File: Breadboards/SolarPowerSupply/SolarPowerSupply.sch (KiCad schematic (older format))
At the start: 47 parts

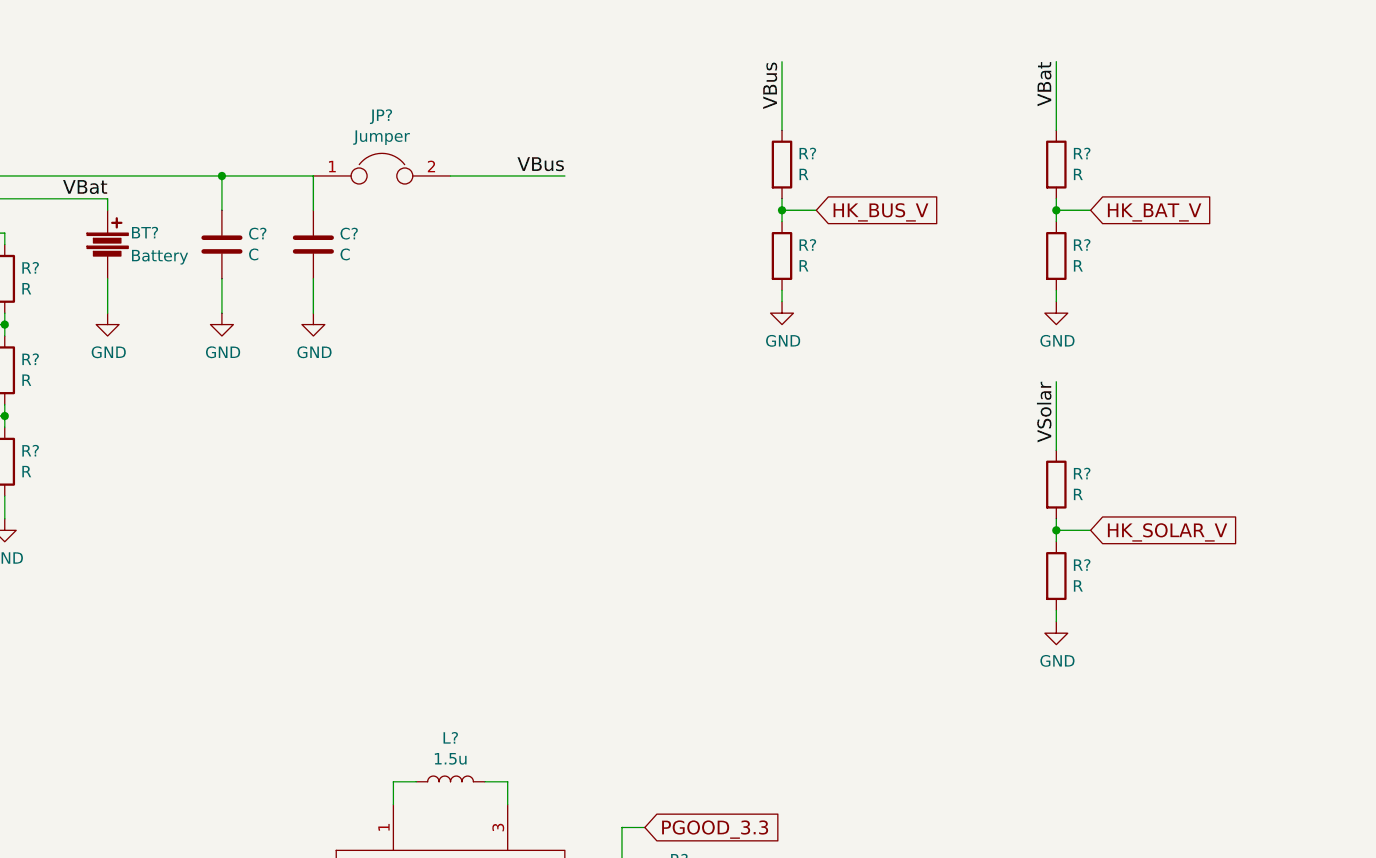
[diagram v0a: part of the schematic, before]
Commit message: Adds Connectors for Power and HK
- One Connector added with 5V, 3.3V and GND
- One Connector added with all HK lines
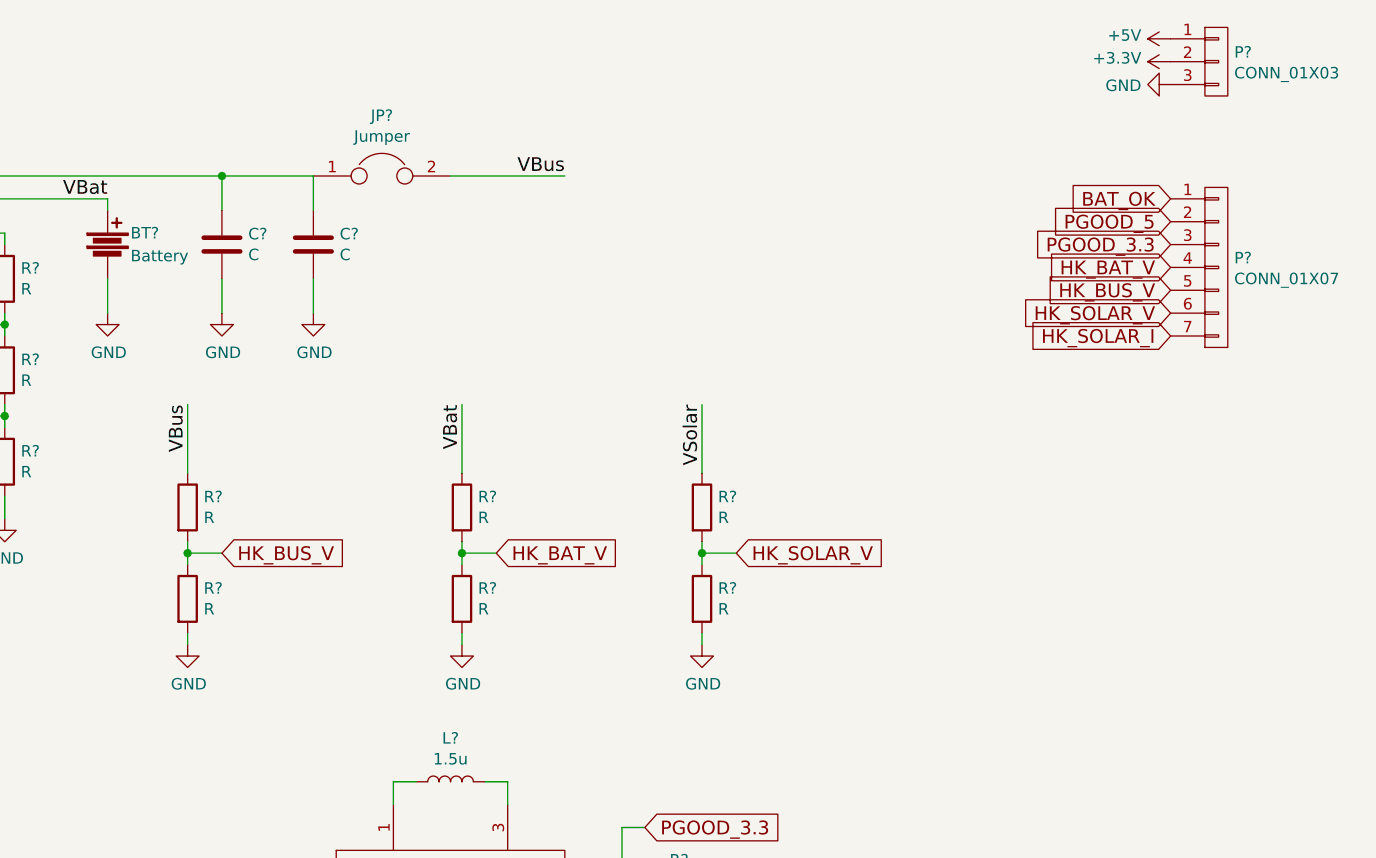
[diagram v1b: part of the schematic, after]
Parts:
- added P?: CONN_01X03, symbol CONN_01X03
- added P?: CONN_01X07, symbol CONN_01X07
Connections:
- net +3V3: now also P?.2 (P2)
- net +5V: now also P?.1 (P1)
- net BAT_OK: now also P?.1 (P1)
- net GND: now also P?.3 (P3)
- net HK_BAT_V: now also P?.4 (P4)
- net HK_BUS_V: now also P?.5 (P5)
- net HK_SOLAR_I: now also P?.7 (P7)
- net HK_SOLAR_V: now also P?.6 (P6)
- net PGOOD_3.3: now also P?.3 (P3)
- net PGOOD_5: now also P?.2 (P2)
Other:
- moved on the sheet: R?
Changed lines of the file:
@@
 L R R?
 U 1 1 5A132406
-P 8650 1600
-F 0 "R?" H 8720 1646 50  0000 L CNN
-F 1 "R" H 8720 1555 50  0000 L CNN
-F 2 "" V 8580 1600 50  0001 C CNN
-F 3 "" H 8650 1600 50  0001 C CNN
-	1    8650 1600
+P 6050 3100
+F 0 "R?" H 6120 3146 50  0000 L CNN
+F 1 "R" H 6120 3055 50  0000 L CNN
+F 2 "" V 5980 3100 50  0001 C CNN
+F 3 "" H 6050 3100 50  0001 C CNN
+	1    6050 3100
 	1    0    0    -1
 $EndComp
@@
 L R R?
 U 1 1 5A132407
-P 8650 2000
-F 0 "R?" H 8720 2046 50  0000 L CNN
-F 1 "R" H 8720 1955 50  0000 L CNN
-F 2 "" V 8580 2000 50  0001 C CNN
-F 3 "" H 8650 2000 50  0001 C CNN
-	1    8650 2000
-	1    0    0    -1
-$EndComp
-Wire Wire Line
-	8650 1150 8650 1450
-Wire Wire Line
-	8650 1750 8650 1850
-Wire Wire Line
-	8650 2150 8650 2200
+P 6050 3500
+F 0 "R?" H 6120 3546 50  0000 L CNN
+F 1 "R" H 6120 3455 50  0000 L CNN
+F 2 "" V 5980 3500 50  0001 C CNN
+F 3 "" H 6050 3500 50  0001 C CNN
+	1    6050 3500
+	1    0    0    -1
+$EndComp
+Wire Wire Line
+	6050 2650 6050 2950
+Wire Wire Line
+	6050 3250 6050 3350
+Wire Wire Line
+	6050 3650 6050 3700
 $Comp
 L GND #PWR?
 U 1 1 5A132408
-P 8650 2200
-F 0 "#PWR?" H 8650 1950 50  0001 C CNN
-F 1 "GND" H 8655 2027 50  0000 C CNN
-F 2 "" H 8650 2200 50  0001 C CNN
-F 3 "" H 8650 2200 50  0001 C CNN
-	1    8650 2200
-	1    0    0    -1
-$EndComp
-Text GLabel 8800 1800 2    60   Input ~ 0
+P 6050 3700
+F 0 "#PWR?" H 6050 3450 50  0001 C CNN
+F 1 "GND" H 6055 3527 50  0000 C CNN
+F 2 "" H 6050 3700 50  0001 C CNN
+F 3 "" H 6050 3700 50  0001 C CNN
+	1    6050 3700
+	1    0    0    -1
+$EndComp
+Text GLabel 6200 3300 2    60   Input ~ 0
 HK_BUS_V
 Wire Wire Line
-	8650 1800 8800 1800
-Connection ~ 8650 1800
-Text Label 8650 1150 3    60   ~ 0
+	6050 3300 6200 3300
+Connection ~ 6050 3300
+Text Label 6050 2650 3    60   ~ 0
 VBus
 $Comp
 L R R?
 U 1 1 5A132409
-P 9850 1600
-F 0 "R?" H 9920 1646 50  0000 L CNN
-F 1 "R" H 9920 1555 50  0000 L CNN
-F 2 "" V 9780 1600 50  0001 C CNN
-F 3 "" H 9850 1600 50  0001 C CNN
-	1    9850 1600
+P 7250 3100
+F 0 "R?" H 7320 3146 50  0000 L CNN
+F 1 "R" H 7320 3055 50  0000 L CNN
+F 2 "" V 7180 3100 50  0001 C CNN
+F 3 "" H 7250 3100 50  0001 C CNN
+	1    7250 3100
 	1    0    0    -1
 $EndComp
@@
 L R R?
 U 1 1 5A13240A
-P 9850 2000
-F 0 "R?" H 9920 2046 50  0000 L CNN
-F 1 "R" H 9920 1955 50  0000 L CNN
-F 2 "" V 9780 2000 50  0001 C CNN
-F 3 "" H 9850 2000 50  0001 C CNN
-	1    9850 2000
-	1    0    0    -1
-$EndComp
-Wire Wire Line
-	9850 1150 9850 1450
-Wire Wire Line
-	9850 1750 9850 1850
-Wire Wire Line
-	9850 2150 9850 2200
+P 7250 3500
+F 0 "R?" H 7320 3546 50  0000 L CNN
+F 1 "R" H 7320 3455 50  0000 L CNN
+F 2 "" V 7180 3500 50  0001 C CNN
+F 3 "" H 7250 3500 50  0001 C CNN
+	1    7250 3500
+	1    0    0    -1
+$EndComp
+Wire Wire Line
+	7250 2650 7250 2950
+Wire Wire Line
+	7250 3250 7250 3350
+Wire Wire Line
+	7250 3650 7250 3700
 $Comp
 L GND #PWR?
 U 1 1 5A13240B
-P 9850 2200
-F 0 "#PWR?" H 9850 1950 50  0001 C CNN
-F 1 "GND" H 9855 2027 50  0000 C CNN
-F 2 "" H 9850 2200 50  0001 C CNN
-F 3 "" H 9850 2200 50  0001 C CNN
-	1    9850 2200
-	1    0    0    -1
-$EndComp
-Text GLabel 10000 1800 2    60   Input ~ 0
+P 7250 3700
+F 0 "#PWR?" H 7250 3450 50  0001 C CNN
+F 1 "GND" H 7255 3527 50  0000 C CNN
+F 2 "" H 7250 3700 50  0001 C CNN
+F 3 "" H 7250 3700 50  0001 C CNN
+	1    7250 3700
+	1    0    0    -1
+$EndComp
+Text GLabel 7400 3300 2    60   Input ~ 0
 HK_BAT_V
 Wire Wire Line
-	9850 1800 10000 1800
-Connection ~ 9850 1800
-Text Label 9850 1150 3    60   ~ 0
+	7250 3300 7400 3300
+Connection ~ 7250 3300
+Text Label 7250 2650 3    60   ~ 0
 VBat
 $Comp
 L R R?
 U 1 1 5A13240C
-P 9850 3000
-F 0 "R?" H 9920 3046 50  0000 L CNN
-F 1 "R" H 9920 2955 50  0000 L CNN
-F 2 "" V 9780 3000 50  0001 C CNN
-F 3 "" H 9850 3000 50  0001 C CNN
-	1    9850 3000
+P 8300 3100
+F 0 "R?" H 8370 3146 50  0000 L CNN
+F 1 "R" H 8370 3055 50  0000 L CNN
+F 2 "" V 8230 3100 50  0001 C CNN
+F 3 "" H 8300 3100 50  0001 C CNN
+	1    8300 3100
 	1    0    0    -1
 $EndComp
@@
 L R R?
 U 1 1 5A13240D
-P 9850 3400
-F 0 "R?" H 9920 3446 50  0000 L CNN
-F 1 "R" H 9920 3355 50  0000 L CNN
-F 2 "" V 9780 3400 50  0001 C CNN
-F 3 "" H 9850 3400 50  0001 C CNN
-	1    9850 3400
-	1    0    0    -1
-$EndComp
-Wire Wire Line
-	9850 2550 9850 2850
-Wire Wire Line
-	9850 3150 9850 3250
-Wire Wire Line
-	9850 3550 9850 3600
+P 8300 3500
+F 0 "R?" H 8370 3546 50  0000 L CNN
+F 1 "R" H 8370 3455 50  0000 L CNN
+F 2 "" V 8230 3500 50  0001 C CNN
+F 3 "" H 8300 3500 50  0001 C CNN
+	1    8300 3500
+	1    0    0    -1
+$EndComp
+Wire Wire Line
+	8300 2650 8300 2950
+Wire Wire Line
+	8300 3250 8300 3350
+Wire Wire Line
+	8300 3650 8300 3700
 $Comp
 L GND #PWR?
 U 1 1 5A13240E
-P 9850 3600
-F 0 "#PWR?" H 9850 3350 50  0001 C CNN
-F 1 "GND" H 9855 3427 50  0000 C CNN
-F 2 "" H 9850 3600 50  0001 C CNN
-F 3 "" H 9850 3600 50  0001 C CNN
-	1    9850 3600
-	1    0    0    -1
-$EndComp
-Text GLabel 10000 3200 2    60   Input ~ 0
+P 8300 3700
+F 0 "#PWR?" H 8300 3450 50  0001 C CNN
+F 1 "GND" H 8305 3527 50  0000 C CNN
+F 2 "" H 8300 3700 50  0001 C CNN
+F 3 "" H 8300 3700 50  0001 C CNN
+	1    8300 3700
+	1    0    0    -1
+$EndComp
+Text GLabel 8450 3300 2    60   Input ~ 0
 HK_SOLAR_V
 Wire Wire Line
-	9850 3200 10000 3200
-Connection ~ 9850 3200
-Text Label 9850 2550 3    60   ~ 0
+	8300 3300 8450 3300
+Connection ~ 8300 3300
+Text Label 8300 2650 3    60   ~ 0
 VSolar
 Text Notes -1050 2700 0    60   Italic 0
@@
 Wire Wire Line
 	1650 3950 1650 4050
+$Comp
+L CONN_01X03 P?
+U 1 1 5A1337CA
+P 10550 1150
+F 0 "P?" H 10628 1191 50  0000 L CNN
+F 1 "CONN_01X03" H 10628 1100 50  0000 L CNN
+F 2 "" H 10550 1150 50  0000 C CNN
+F 3 "" H 10550 1150 50  0000 C CNN
+	1    10550 1150
+	1    0    0    -1
+$EndComp
+$Comp
+L +3.3V #PWR?
+U 1 1 5A1339BF
+P 10350 1150
+F 0 "#PWR?" H 10350 1000 50  0001 C CNN
+F 1 "+3.3V" V 10365 1278 50  0000 L CNN
+F 2 "" H 10350 1150 50  0000 C CNN
+F 3 "" H 10350 1150 50  0000 C CNN
+	1    10350 1150
+	0    -1   -1   0
+$EndComp
+$Comp
+L +5V #PWR?
+U 1 1 5A133B1D
+P 10350 1050
+F 0 "#PWR?" H 10350 900 50  0001 C CNN
+F 1 "+5V" V 10365 1178 50  0000 L CNN
+F 2 "" H 10350 1050 50  0000 C CNN
+F 3 "" H 10350 1050 50  0000 C CNN
+	1    10350 1050
+	0    -1   -1   0
+$EndComp
+$Comp
+L CONN_01X07 P?
+U 1 1 5A1343A8
+P 10550 2050
+F 0 "P?" H 10628 2091 50  0000 L CNN
+F 1 "CONN_01X07" H 10628 2000 50  0000 L CNN
+F 2 "" H 10550 2050 50  0000 C CNN
+F 3 "" H 10550 2050 50  0000 C CNN
+	1    10550 2050
+	1    0    0    -1
+$EndComp
+$Comp
+L GND #PWR?
+U 1 1 5A1344E4
+P 10350 1250
+F 0 "#PWR?" H 10350 1000 50  0001 C CNN
+F 1 "GND" V 10355 1122 50  0000 R CNN
+F 2 "" H 10350 1250 50  0000 C CNN
+F 3 "" H 10350 1250 50  0000 C CNN
+	1    10350 1250
+	0    1    1    0
+$EndComp
+Text GLabel 10350 1750 0    60   Input ~ 0
+BAT_OK
+Text GLabel 10350 1950 0    60   Input ~ 0
+PGOOD_3.3
+Text GLabel 10350 1850 0    60   Input ~ 0
+PGOOD_5
+Text GLabel 10350 2350 0    60   Input ~ 0
+HK_SOLAR_I
+Text GLabel 10350 2050 0    60   Input ~ 0
+HK_BAT_V
+Text GLabel 10350 2150 0    60   Input ~ 0
+HK_BUS_V
+Text GLabel 10350 2250 0    60   Input ~ 0
+HK_SOLAR_V
 $EndSCHEMATC

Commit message: Annotates PowerSupply BB
- All components are annotated
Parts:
- gave numbers to parts that had none: 49

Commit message: Mapped all symbols to Footprint
- Also added Mouser Part Number (MPN) where applicable as a field.
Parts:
- BT101: footprint Connectors_Molex:Molex_KK-6410-02_02x2.54mm_Straight -> Octanis3:TE_282834-2; MPN (none) -> 571-282834-2
- C101: value C -> 4.7u; footprint (none) -> Octanis3:C_SMD_2012_Hand; MPN (none) -> 81-GRM21R61A475KE34D; Tolerance (none) -> 10%
- C102: value C -> 100n; footprint (none) -> Capacitors_SMD:C_0603_HandSoldering
- C103: value C -> 10n; footprint (none) -> Capacitors_SMD:C_0603_HandSoldering; Tolerance (none) -> 10%
- C104, C105, C106, C107, C108, C109: footprint (none) -> Octanis3:C_SMD_2012_Hand; MPN (none) -> 81-GRM21BR61C106KE5K
- C110: footprint (none) -> Capacitors_SMD:C_0603_HandSoldering
- D101, D102: footprint (none) -> LEDs:LED_0603_HandSoldering
- JP101, JP102, JP103, JP104, JP105: footprint (none) -> Pin_Headers:Pin_Header_Straight_1x02_Pitch2.54mm
- L101: value L -> 22u; footprint (none) -> Inductors_SMD:L_Wuerth_WE-TPC-3816; MPN (none) -> 710-744031220; Tolerance (none) -> 20%
- L102, L103: footprint (none) -> Octanis3:L_2520_HandSoldering; MPN (none) -> 81-1269AS-H-1R5MP2
- P101: footprint (none) -> Pin_Headers:Pin_Header_Straight_1x03_Pitch2.54mm
- P102: footprint (none) -> Pin_Headers:Pin_Header_Straight_1x07_Pitch2.54mm
- R101, R102, R103, R104, R105, R106, R108, R109, R110, R111, R112, R113, R114, R115, R116, R117, R118, R119, R120, R121, R122: footprint (none) -> Resistors_SMD:R_0603_HandSoldering
- R107: footprint (none) -> Resistors_SMD:R_1206_HandSoldering
- SC101: footprint (none) -> Octanis3:TE_282834-2; Mouser-Part (none) -> 571-282834-2
- U101: footprint (none) -> Housings_DFN_QFN:QFN-16-1EP_3x3mm_Pitch0.5mm_ThermalVias
- U102, U103: footprint (none) -> Octanis3:VQFN_12_2.5x2.5mm

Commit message: Updates bg25504 symbol and connects 5V-enable
- The new schematic symbol for the bq25504 was added in the breadboard,
  now including the ground pad.
- The 5V Enable signals was routed out onto a connector.
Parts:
- removed P101: CONN_01X03, Pin_Headers:Pin_Header_Straight_1x03_Pitch2.54mm, symbol CONN_01X03
- added P101: CONN_01X04, Pin_Headers:Pin_Header_Straight_1x04_Pitch2.54mm, symbol CONN_01X04
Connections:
- net +3V3: now also P101.3 (P3)
- net +5V: now also P101.2 (P2)
- net 5V_Enable: now also P101.1 (P1)
- net GND: now also U101.13 (VSS), P101.4 (P4)
- net at C103.1: now also U101.4 (VREF_SAMP)
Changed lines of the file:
@@
 	2750 2250 2600 2250
 Wire Wire Line
-	2600 2250 2600 2550
+	2600 2150 2600 2550
 $Comp
 L GND #PWR01
@@
 	2350 2400 2350 2550
 Wire Wire Line
-	2750 2050 2350 2050
-Wire Wire Line
-	2350 2050 2350 2100
+	2350 1950 2350 2100
 Connection ~ 2050 1600
 $Comp
@@
 Wire Wire Line
 	1650 3950 1650 4050
-$Comp
-L CONN_01X03 P101
-U 1 1 5A1337CA
-P 10550 1150
-F 0 "P101" H 10628 1191 50  0000 L CNN
-F 1 "CONN_01X03" H 10628 1100 50  0000 L CNN
-F 2 "Pin_Headers:Pin_Header_Straight_1x03_Pitch2.54mm" H 10550 1150 50  0001 C CNN
-F 3 "" H 10550 1150 50  0000 C CNN
-	1    10550 1150
-	1    0    0    -1
-$EndComp
 $Comp
 L +3.3V #PWR030
@@
 Text GLabel 10350 2250 0    60   Input ~ 0
 HK_SOLAR_V
+Wire Wire Line
+	2750 1950 2350 1950
+Wire Wire Line
+	2600 2150 2750 2150
+Connection ~ 2600 2250
+$Comp
+L CONN_01X04 P101
+U 1 1 5A14746F
+P 10550 1100
+F 0 "P101" H 10628 1141 50  0000 L CNN
+F 1 "CONN_01X04" H 10628 1050 50  0000 L CNN
+F 2 "Pin_Headers:Pin_Header_Straight_1x04_Pitch2.54mm" H 10550 1100 50  0001 C CNN
+F 3 "" H 10550 1100 50  0000 C CNN
+	1    10550 1100
+	1    0    0    -1
+$EndComp
+Text GLabel 10350 950  0    60   Input ~ 0
+5V_Enable
 $EndSCHEMATC

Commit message: Ensures Design mostly DRC clean
Removed remaining DRC errors, mostly copper traces too close.
Some DRC errors remain, within the SOIC-16 package of the bq25504,
     "PADS TOO CLOSE" -> to be ignored.
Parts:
- U101: footprint Housings_DFN_QFN:QFN-16-1EP_3x3mm_Pitch0.5mm_ThermalVias -> Housings_DFN_QFN:QFN-16-1EP_3x3mm_Pitch0.5mm
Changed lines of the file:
@@
 F 0 "U101" H 3500 1587 60  0000 C CNN
 F 1 "bq25504" H 3500 1481 60  0000 C CNN
-F 2 "Housings_DFN_QFN:QFN-16-1EP_3x3mm_Pitch0.5mm_ThermalVias" H 2950 1400 60  0001 C CNN
+F 2 "Housings_DFN_QFN:QFN-16-1EP_3x3mm_Pitch0.5mm" H 2950 1400 60  0001 C CNN
 F 3 "" H 2950 1400 60  0001 C CNN
 	1    2950 1400
